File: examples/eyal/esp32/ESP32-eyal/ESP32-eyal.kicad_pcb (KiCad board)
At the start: 2 copper layers, 47 x 45.7 mm, 30 parts, among them J1 Battery, J2 OW, J3 V1, J4 Serial, J5 VDD_I_SENSE, J6 BATT_I_SENSE, J7 ALT_V2, J8 ALT_V3, J9 Solar, Q1 2N7002W, Q2 DMP1045U, Q3 DMP1045U, Q4 DMP1045U, U1 RT9080-33, U2 ESP32-WROOM-32, U3 MCP73831

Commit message: Commit recent updates
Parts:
- added R12: 10K, Resistor_SMD:R_0805_2012Metric, F.Cu at (98.4, 107.3)
- J4: footprint Connector_PinHeader_2.54mm:PinHeader_1x03_P2.54mm_Vertical -> Connector_PinHeader_2.54mm:PinHeader_1x05_P2.54mm_Vertical
- moved J4 5.12 mm to (139.1, 139.1)
- moved Program1 0.90 mm to (123.2, 125.1)
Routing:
- net /EN: track 24.0 -> 76.7 mm, vias 0 -> 1
- net /PGM: track 4.71 -> 24.5 mm, vias 0 -> 1
- net Net-(J4-Pad1): track 36.8 -> 41.4 mm
- net Net-(J4-Pad3): track 31.1 -> 35.6 mm
- net /SOLAR: track 7.41 -> 9.26 mm
- net VDD: track 107.0 -> 108.7 mm
- net /V1: track 42.6 -> 43.9 mm
- net +BATT: track 77.3 -> 78.5 mm
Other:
- board text added: "DTR"
- board text added: "RTS"

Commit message: some minor pcb adjustments (clear DRC warnings).
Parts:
- moved R10 0.64 mm to (139.7, 124.5)
- moved R7 0.64 mm to (137.2, 124.5)
- moved J4 0.63 mm to (139.1, 138.4)
- renumbered Program1 to pgm, Reset1 to rst
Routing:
- net Net-(J4-Pad1): track 41.4 -> 39.1 mm
- net Net-(J4-Pad3): track 35.6 -> 33.5 mm
- net GND: track 213.2 -> 211.6 mm
- net +BATT: track 78.5 -> 76.9 mm
- net /VDD_SENSE: track 51.3 -> 49.9 mm
- net VDD: track 108.7 -> 107.5 mm
- net /VBAT_SENSE: track 46.1 -> 47.2 mm
- net /V1_SENSE: track 53.9 -> 53.2 mm
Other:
- board size 47 x 45.7 mm -> 47.6 x 46.4 mm
- board text added: "SCL"
- board text added: "SDA"
- board text added: "SOLR"
- board text removed: "OW"

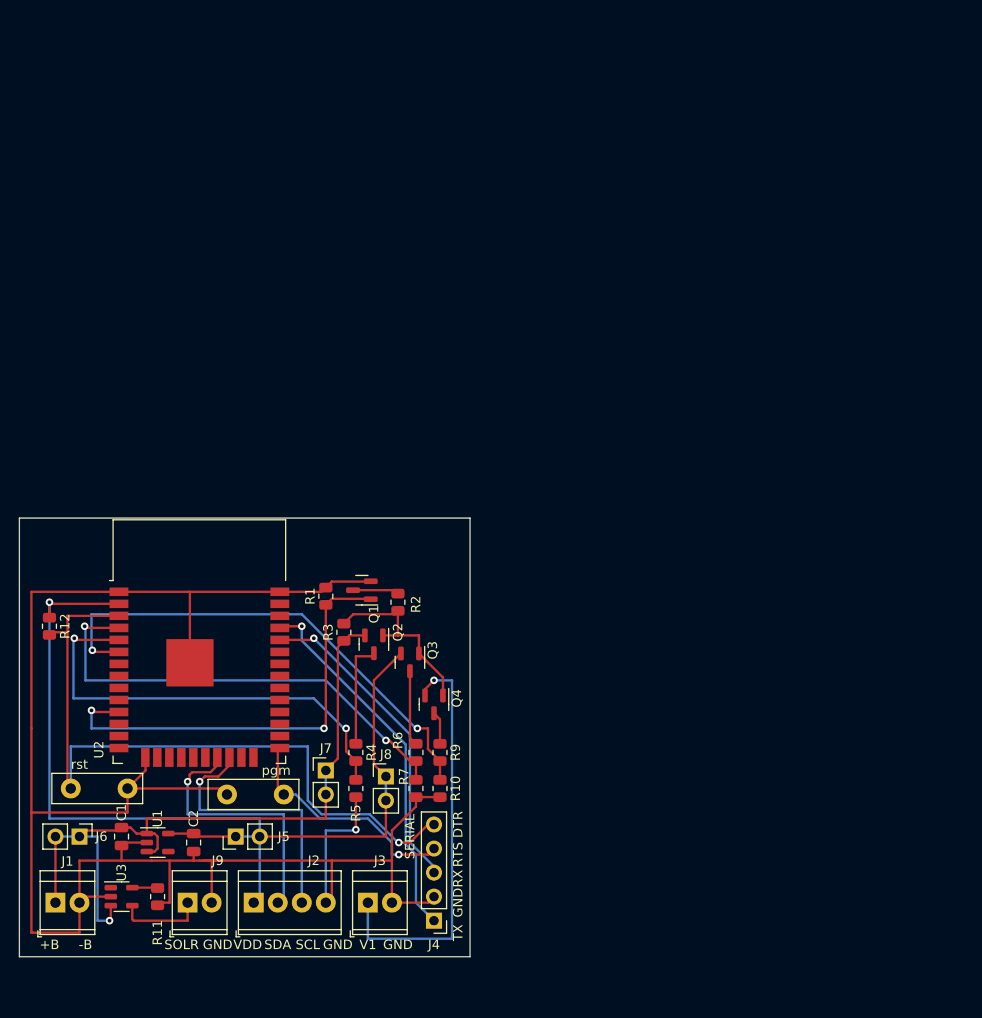
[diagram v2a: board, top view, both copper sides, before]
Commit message: Same ESP pcb with many other small sot-23 adapters.
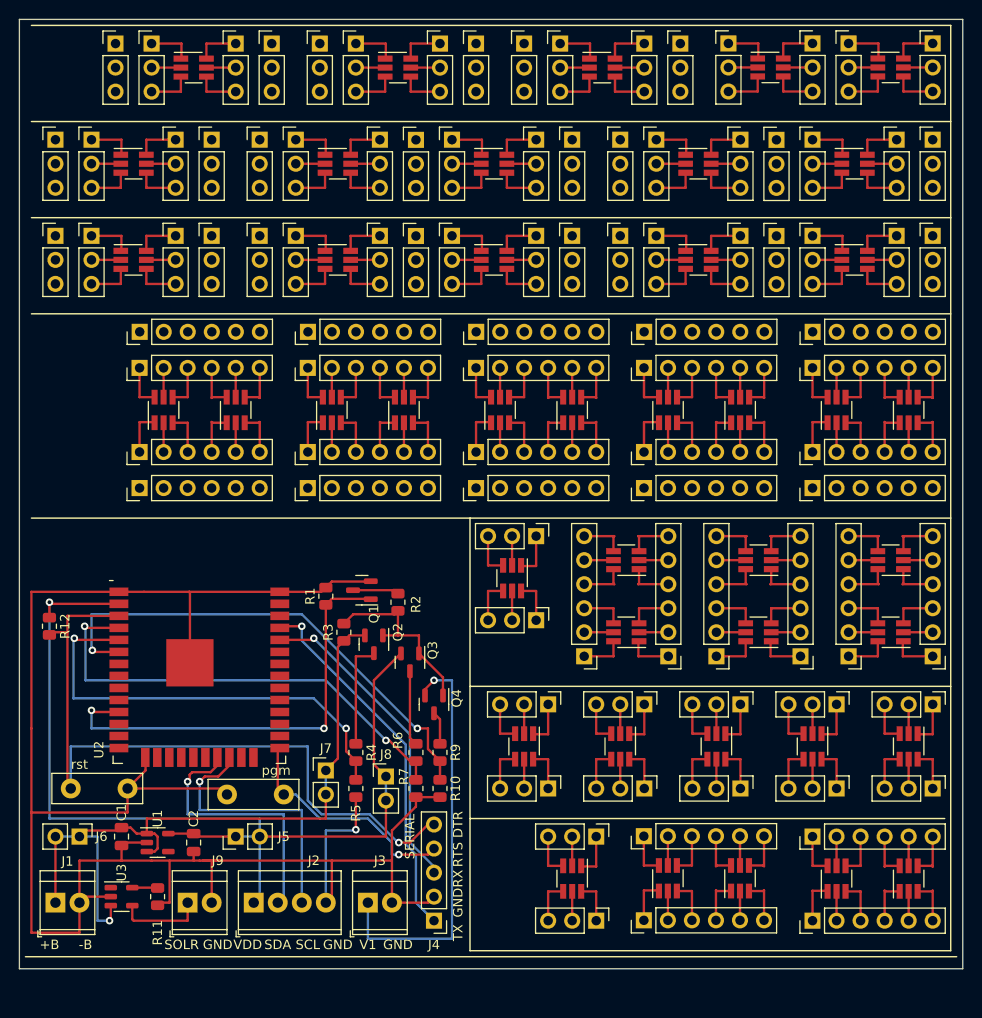
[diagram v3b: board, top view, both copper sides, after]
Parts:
- added REF**: PinHeader_1x03_P2.54mm_Vertical, Connector_PinHeader_2.54mm:PinHeader_1x03_P2.54mm_Vertical, F.Cu at (161.3, 115.6)
- added REF**: PinHeader_1x06_P2.54mm_Vertical, Connector_PinHeader_2.54mm:PinHeader_1x06_P2.54mm_Vertical, F.Cu at (108.0, 88.9)
- added REF**: PinHeader_1x03_P2.54mm_Vertical, Connector_PinHeader_2.54mm:PinHeader_1x03_P2.54mm_Vertical, F.Cu at (156.2, 138.4)
- added REF**: PinHeader_1x03_P2.54mm_Vertical, Connector_PinHeader_2.54mm:PinHeader_1x03_P2.54mm_Vertical, F.Cu at (162.6, 66.1)
- added REF**: PinHeader_1x03_P2.54mm_Vertical, Connector_PinHeader_2.54mm:PinHeader_1x03_P2.54mm_Vertical, F.Cu at (102.9, 55.9)
- added REF**: PinHeader_1x06_P2.54mm_Vertical, Connector_PinHeader_2.54mm:PinHeader_1x06_P2.54mm_Vertical, F.Cu at (161.2, 138.4)
- added REF**: PinHeader_1x06_P2.54mm_Vertical, Connector_PinHeader_2.54mm:PinHeader_1x06_P2.54mm_Vertical, F.Cu at (143.5, 80.0)
- added REF**: PinHeader_1x03_P2.54mm_Vertical, Connector_PinHeader_2.54mm:PinHeader_1x03_P2.54mm_Vertical, F.Cu at (149.9, 106.7)
- added REF**: PinHeader_1x06_P2.54mm_Vertical, Connector_PinHeader_2.54mm:PinHeader_1x06_P2.54mm_Vertical, F.Cu at (191.8, 110.5)
- added REF**: PinHeader_1x06_P2.54mm_Vertical, Connector_PinHeader_2.54mm:PinHeader_1x06_P2.54mm_Vertical, F.Cu at (182.9, 110.5)
- added REF**: PinHeader_1x03_P2.54mm_Vertical, Connector_PinHeader_2.54mm:PinHeader_1x03_P2.54mm_Vertical, F.Cu at (161.3, 124.5)
- added REF**: PinHeader_1x03_P2.54mm_Vertical, Connector_PinHeader_2.54mm:PinHeader_1x03_P2.54mm_Vertical, F.Cu at (124.5, 66.1)
- added REF**: SOT-23-6_Handsoldering, Package_TO_SOT_SMD:SOT-23-6_Handsoldering, F.Cu at (168.9, 120.0)
- added REF**: PinHeader_1x06_P2.54mm_Vertical, Connector_PinHeader_2.54mm:PinHeader_1x06_P2.54mm_Vertical, F.Cu at (179.1, 92.7)
- added REF**: PinHeader_1x03_P2.54mm_Vertical, Connector_PinHeader_2.54mm:PinHeader_1x03_P2.54mm_Vertical, F.Cu at (118.1, 45.7)
- added REF**: PinHeader_1x03_P2.54mm_Vertical, Connector_PinHeader_2.54mm:PinHeader_1x03_P2.54mm_Vertical, F.Cu at (171.4, 55.9)
- added REF**: SOT-23-6_Handsoldering, Package_TO_SOT_SMD:SOT-23-6_Handsoldering, F.Cu at (107.3, 58.4)
- added REF**: PinHeader_1x03_P2.54mm_Vertical, Connector_PinHeader_2.54mm:PinHeader_1x03_P2.54mm_Vertical, F.Cu at (191.8, 124.5)
- added REF**: PinHeader_1x06_P2.54mm_Vertical, Connector_PinHeader_2.54mm:PinHeader_1x06_P2.54mm_Vertical, F.Cu at (161.3, 92.7)
- added REF**: SOT-23-6_Handsoldering, Package_TO_SOT_SMD:SOT-23-6_Handsoldering, F.Cu at (128.9, 58.4)
- added REF**: SOT-23-6_Handsoldering, Package_TO_SOT_SMD:SOT-23-6_Handsoldering, F.Cu at (173.4, 108.0)
- added REF**: PinHeader_1x06_P2.54mm_Vertical, Connector_PinHeader_2.54mm:PinHeader_1x06_P2.54mm_Vertical, F.Cu at (179.1, 76.2)
- added REF**: SOT-23-6_Handsoldering, Package_TO_SOT_SMD:SOT-23-6_Handsoldering, F.Cu at (135.9, 84.5)
- added REF**: SOT-23-6_Handsoldering, Package_TO_SOT_SMD:SOT-23-6_Handsoldering, F.Cu at (163.8, 84.5)
- added REF**: PinHeader_1x03_P2.54mm_Vertical, Connector_PinHeader_2.54mm:PinHeader_1x03_P2.54mm_Vertical, F.Cu at (182.9, 45.7)
- added REF**: PinHeader_1x03_P2.54mm_Vertical, Connector_PinHeader_2.54mm:PinHeader_1x03_P2.54mm_Vertical, F.Cu at (161.3, 45.7)
- added REF**: PinHeader_1x03_P2.54mm_Vertical, Connector_PinHeader_2.54mm:PinHeader_1x03_P2.54mm_Vertical, F.Cu at (171.4, 66.1)
- added REF**: SOT-23-6_Handsoldering, Package_TO_SOT_SMD:SOT-23-6_Handsoldering, F.Cu at (118.1, 84.5)
- added REF**: PinHeader_1x06_P2.54mm_Vertical, Connector_PinHeader_2.54mm:PinHeader_1x06_P2.54mm_Vertical, F.Cu at (108.0, 76.2)
- added REF**: SOT-23-6_Handsoldering, Package_TO_SOT_SMD:SOT-23-6_Handsoldering, F.Cu at (147.3, 102.2)
- added REF**: PinHeader_1x03_P2.54mm_Vertical, Connector_PinHeader_2.54mm:PinHeader_1x03_P2.54mm_Vertical, F.Cu at (111.8, 55.9)
- added REF**: SOT-23-6_Handsoldering, Package_TO_SOT_SMD:SOT-23-6_Handsoldering, F.Cu at (179.1, 120.0)
- added REF**: PinHeader_1x03_P2.54mm_Vertical, Connector_PinHeader_2.54mm:PinHeader_1x03_P2.54mm_Vertical, F.Cu at (179.1, 55.9)
- added REF**: PinHeader_1x03_P2.54mm_Vertical, Connector_PinHeader_2.54mm:PinHeader_1x03_P2.54mm_Vertical, F.Cu at (139.7, 45.7)
- added REF**: PinHeader_1x06_P2.54mm_Vertical, Connector_PinHeader_2.54mm:PinHeader_1x06_P2.54mm_Vertical, F.Cu at (125.7, 88.9)
- added REF**: SOT-23-6_Handsoldering, Package_TO_SOT_SMD:SOT-23-6_Handsoldering, F.Cu at (173.4, 100.3)
- added REF**: PinHeader_1x03_P2.54mm_Vertical, Connector_PinHeader_2.54mm:PinHeader_1x03_P2.54mm_Vertical, F.Cu at (149.9, 55.9)
- added REF**: PinHeader_1x03_P2.54mm_Vertical, Connector_PinHeader_2.54mm:PinHeader_1x03_P2.54mm_Vertical, F.Cu at (99.1, 55.9)
- added REF**: PinHeader_1x03_P2.54mm_Vertical, Connector_PinHeader_2.54mm:PinHeader_1x03_P2.54mm_Vertical, F.Cu at (151.1, 124.5)
- added REF**: SOT-23-6_Handsoldering, Package_TO_SOT_SMD:SOT-23-6_Handsoldering, F.Cu at (187.3, 48.3)
- added REF**: SOT-23-6_Handsoldering, Package_TO_SOT_SMD:SOT-23-6_Handsoldering, F.Cu at (187.3, 100.3)
- added REF**: SOT-23-6_Handsoldering, Package_TO_SOT_SMD:SOT-23-6_Handsoldering, F.Cu at (110.5, 84.5)
- added REF**: PinHeader_1x06_P2.54mm_Vertical, Connector_PinHeader_2.54mm:PinHeader_1x06_P2.54mm_Vertical, F.Cu at (143.5, 92.7)
- added REF**: SOT-23-6_Handsoldering, Package_TO_SOT_SMD:SOT-23-6_Handsoldering, F.Cu at (128.9, 68.6)
- added REF**: SOT-23-6_Handsoldering, Package_TO_SOT_SMD:SOT-23-6_Handsoldering, F.Cu at (171.4, 84.5)
- added REF**: SOT-23-6_Handsoldering, Package_TO_SOT_SMD:SOT-23-6_Handsoldering, F.Cu at (153.7, 134.0)
- added REF**: PinHeader_1x03_P2.54mm_Vertical, Connector_PinHeader_2.54mm:PinHeader_1x03_P2.54mm_Vertical, F.Cu at (133.3, 66.1)
- added REF**: PinHeader_1x06_P2.54mm_Vertical, Connector_PinHeader_2.54mm:PinHeader_1x06_P2.54mm_Vertical, F.Cu at (154.9, 110.5)
- added REF**: SOT-23-6_Handsoldering, Package_TO_SOT_SMD:SOT-23-6_Handsoldering, F.Cu at (167.0, 58.4)
- added REF**: PinHeader_1x06_P2.54mm_Vertical, Connector_PinHeader_2.54mm:PinHeader_1x06_P2.54mm_Vertical, F.Cu at (179.1, 129.5)
- added REF**: PinHeader_1x06_P2.54mm_Vertical, Connector_PinHeader_2.54mm:PinHeader_1x06_P2.54mm_Vertical, F.Cu at (108.0, 92.7)
- added REF**: PinHeader_1x03_P2.54mm_Vertical, Connector_PinHeader_2.54mm:PinHeader_1x03_P2.54mm_Vertical, F.Cu at (141.0, 55.9)
- added REF**: PinHeader_1x03_P2.54mm_Vertical, Connector_PinHeader_2.54mm:PinHeader_1x03_P2.54mm_Vertical, F.Cu at (133.3, 55.9)
- added REF**: PinHeader_1x03_P2.54mm_Vertical, Connector_PinHeader_2.54mm:PinHeader_1x03_P2.54mm_Vertical, F.Cu at (179.1, 66.1)
- added REF**: PinHeader_1x03_P2.54mm_Vertical, Connector_PinHeader_2.54mm:PinHeader_1x03_P2.54mm_Vertical, F.Cu at (149.9, 97.8)
- added REF**: PinHeader_1x06_P2.54mm_Vertical, Connector_PinHeader_2.54mm:PinHeader_1x06_P2.54mm_Vertical, F.Cu at (161.3, 76.2)
- added REF**: PinHeader_1x06_P2.54mm_Vertical, Connector_PinHeader_2.54mm:PinHeader_1x06_P2.54mm_Vertical, F.Cu at (177.8, 110.5)
- added REF**: PinHeader_1x03_P2.54mm_Vertical, Connector_PinHeader_2.54mm:PinHeader_1x03_P2.54mm_Vertical, F.Cu at (181.6, 115.6)
- added REF**: PinHeader_1x06_P2.54mm_Vertical, Connector_PinHeader_2.54mm:PinHeader_1x06_P2.54mm_Vertical, F.Cu at (163.8, 110.5)
- added REF**: PinHeader_1x06_P2.54mm_Vertical, Connector_PinHeader_2.54mm:PinHeader_1x06_P2.54mm_Vertical, F.Cu at (143.5, 76.2)
- added REF**: SOT-23-6_Handsoldering, Package_TO_SOT_SMD:SOT-23-6_Handsoldering, F.Cu at (107.3, 68.6)
- added REF**: PinHeader_1x06_P2.54mm_Vertical, Connector_PinHeader_2.54mm:PinHeader_1x06_P2.54mm_Vertical, F.Cu at (161.3, 80.0)
- added REF**: PinHeader_1x03_P2.54mm_Vertical, Connector_PinHeader_2.54mm:PinHeader_1x03_P2.54mm_Vertical, F.Cu at (171.4, 124.5)
- added REF**: PinHeader_1x03_P2.54mm_Vertical, Connector_PinHeader_2.54mm:PinHeader_1x03_P2.54mm_Vertical, F.Cu at (181.6, 124.5)
- added REF**: PinHeader_1x03_P2.54mm_Vertical, Connector_PinHeader_2.54mm:PinHeader_1x03_P2.54mm_Vertical, F.Cu at (153.7, 55.9)
- added REF**: SOT-23-6_Handsoldering, Package_TO_SOT_SMD:SOT-23-6_Handsoldering, F.Cu at (145.4, 58.4)
- added REF**: SOT-23-6_Handsoldering, Package_TO_SOT_SMD:SOT-23-6_Handsoldering, F.Cu at (171.4, 133.9)
- added REF**: SOT-23-6_Handsoldering, Package_TO_SOT_SMD:SOT-23-6_Handsoldering, F.Cu at (189.2, 134.0)
- added REF**: SOT-23-6_Handsoldering, Package_TO_SOT_SMD:SOT-23-6_Handsoldering, F.Cu at (148.6, 120.0)
- added REF**: PinHeader_1x03_P2.54mm_Vertical, Connector_PinHeader_2.54mm:PinHeader_1x03_P2.54mm_Vertical, F.Cu at (153.7, 66.1)
- added REF**: SOT-23-6_Handsoldering, Package_TO_SOT_SMD:SOT-23-6_Handsoldering, F.Cu at (183.5, 58.4)
- added REF**: SOT-23-6_Handsoldering, Package_TO_SOT_SMD:SOT-23-6_Handsoldering, F.Cu at (159.4, 108.0)
- added REF**: PinHeader_1x06_P2.54mm_Vertical, Connector_PinHeader_2.54mm:PinHeader_1x06_P2.54mm_Vertical, F.Cu at (143.5, 88.9)
- added REF**: PinHeader_1x06_P2.54mm_Vertical, Connector_PinHeader_2.54mm:PinHeader_1x06_P2.54mm_Vertical, F.Cu at (161.3, 88.9)
- added REF**: SOT-23-6_Handsoldering, Package_TO_SOT_SMD:SOT-23-6_Handsoldering, F.Cu at (145.4, 68.6)
- added REF**: PinHeader_1x03_P2.54mm_Vertical, Connector_PinHeader_2.54mm:PinHeader_1x03_P2.54mm_Vertical, F.Cu at (170.2, 45.7)
- added REF**: PinHeader_1x03_P2.54mm_Vertical, Connector_PinHeader_2.54mm:PinHeader_1x03_P2.54mm_Vertical, F.Cu at (124.5, 55.9)
- added REF**: PinHeader_1x03_P2.54mm_Vertical, Connector_PinHeader_2.54mm:PinHeader_1x03_P2.54mm_Vertical, F.Cu at (109.2, 45.7)
- added REF**: PinHeader_1x06_P2.54mm_Vertical, Connector_PinHeader_2.54mm:PinHeader_1x06_P2.54mm_Vertical, F.Cu at (179.1, 80.0)
- added REF**: PinHeader_1x03_P2.54mm_Vertical, Connector_PinHeader_2.54mm:PinHeader_1x03_P2.54mm_Vertical, F.Cu at (121.9, 45.7)
- added REF**: PinHeader_1x03_P2.54mm_Vertical, Connector_PinHeader_2.54mm:PinHeader_1x03_P2.54mm_Vertical, F.Cu at (175.3, 55.9)
- added REF**: PinHeader_1x03_P2.54mm_Vertical, Connector_PinHeader_2.54mm:PinHeader_1x03_P2.54mm_Vertical, F.Cu at (171.4, 115.6)
- added REF**: PinHeader_1x06_P2.54mm_Vertical, Connector_PinHeader_2.54mm:PinHeader_1x06_P2.54mm_Vertical, F.Cu at (125.7, 76.2)
- added REF**: PinHeader_1x06_P2.54mm_Vertical, Connector_PinHeader_2.54mm:PinHeader_1x06_P2.54mm_Vertical, F.Cu at (125.7, 92.7)
- added REF**: PinHeader_1x03_P2.54mm_Vertical, Connector_PinHeader_2.54mm:PinHeader_1x03_P2.54mm_Vertical, F.Cu at (120.7, 66.1)
- added REF**: SOT-23-6_Handsoldering, Package_TO_SOT_SMD:SOT-23-6_Handsoldering, F.Cu at (156.8, 48.3)
- added REF**: PinHeader_1x03_P2.54mm_Vertical, Connector_PinHeader_2.54mm:PinHeader_1x03_P2.54mm_Vertical, F.Cu at (127.0, 45.7)
- added REF**: PinHeader_1x03_P2.54mm_Vertical, Connector_PinHeader_2.54mm:PinHeader_1x03_P2.54mm_Vertical, F.Cu at (162.6, 55.9)
- added REF**: PinHeader_1x03_P2.54mm_Vertical, Connector_PinHeader_2.54mm:PinHeader_1x03_P2.54mm_Vertical, F.Cu at (148.6, 45.7)
- added REF**: PinHeader_1x06_P2.54mm_Vertical, Connector_PinHeader_2.54mm:PinHeader_1x06_P2.54mm_Vertical, F.Cu at (179.1, 138.4)
- added REF**: PinHeader_1x03_P2.54mm_Vertical, Connector_PinHeader_2.54mm:PinHeader_1x03_P2.54mm_Vertical, F.Cu at (179.1, 45.7)
- added REF**: PinHeader_1x03_P2.54mm_Vertical, Connector_PinHeader_2.54mm:PinHeader_1x03_P2.54mm_Vertical, F.Cu at (115.6, 66.1)
- added REF**: PinHeader_1x03_P2.54mm_Vertical, Connector_PinHeader_2.54mm:PinHeader_1x03_P2.54mm_Vertical, F.Cu at (120.7, 55.9)
- added REF**: SOT-23-6_Handsoldering, Package_TO_SOT_SMD:SOT-23-6_Handsoldering, F.Cu at (183.5, 68.6)
- added REF**: PinHeader_1x03_P2.54mm_Vertical, Connector_PinHeader_2.54mm:PinHeader_1x03_P2.54mm_Vertical, F.Cu at (165.1, 45.7)
- added REF**: SOT-23-6_Handsoldering, Package_TO_SOT_SMD:SOT-23-6_Handsoldering, F.Cu at (187.3, 108.0)
- added REF**: PinHeader_1x03_P2.54mm_Vertical, Connector_PinHeader_2.54mm:PinHeader_1x03_P2.54mm_Vertical, F.Cu at (191.8, 55.9)
- added REF**: SOT-23-6_Handsoldering, Package_TO_SOT_SMD:SOT-23-6_Handsoldering, F.Cu at (158.8, 120.0)
- added REF**: SOT-23-6_Handsoldering, Package_TO_SOT_SMD:SOT-23-6_Handsoldering, F.Cu at (153.7, 84.5)
- added REF**: PinHeader_1x03_P2.54mm_Vertical, Connector_PinHeader_2.54mm:PinHeader_1x03_P2.54mm_Vertical, F.Cu at (102.9, 66.1)
- added REF**: PinHeader_1x03_P2.54mm_Vertical, Connector_PinHeader_2.54mm:PinHeader_1x03_P2.54mm_Vertical, F.Cu at (152.4, 45.7)
- added REF**: PinHeader_1x06_P2.54mm_Vertical, Connector_PinHeader_2.54mm:PinHeader_1x06_P2.54mm_Vertical, F.Cu at (168.9, 110.5)
- added REF**: PinHeader_1x03_P2.54mm_Vertical, Connector_PinHeader_2.54mm:PinHeader_1x03_P2.54mm_Vertical, F.Cu at (130.8, 45.7)
- added REF**: PinHeader_1x03_P2.54mm_Vertical, Connector_PinHeader_2.54mm:PinHeader_1x03_P2.54mm_Vertical, F.Cu at (149.9, 66.1)
- added REF**: PinHeader_1x03_P2.54mm_Vertical, Connector_PinHeader_2.54mm:PinHeader_1x03_P2.54mm_Vertical, F.Cu at (175.3, 66.1)
- added REF**: PinHeader_1x03_P2.54mm_Vertical, Connector_PinHeader_2.54mm:PinHeader_1x03_P2.54mm_Vertical, F.Cu at (115.6, 55.9)
- added REF**: PinHeader_1x03_P2.54mm_Vertical, Connector_PinHeader_2.54mm:PinHeader_1x03_P2.54mm_Vertical, F.Cu at (188.0, 55.9)
- added REF**: PinHeader_1x03_P2.54mm_Vertical, Connector_PinHeader_2.54mm:PinHeader_1x03_P2.54mm_Vertical, F.Cu at (141.0, 66.1)
- added REF**: PinHeader_1x06_P2.54mm_Vertical, Connector_PinHeader_2.54mm:PinHeader_1x06_P2.54mm_Vertical, F.Cu at (179.1, 88.9)
- added REF**: PinHeader_1x03_P2.54mm_Vertical, Connector_PinHeader_2.54mm:PinHeader_1x03_P2.54mm_Vertical, F.Cu at (105.4, 45.7)
- added REF**: SOT-23-6_Handsoldering, Package_TO_SOT_SMD:SOT-23-6_Handsoldering, F.Cu at (167.0, 68.6)
- added REF**: PinHeader_1x03_P2.54mm_Vertical, Connector_PinHeader_2.54mm:PinHeader_1x03_P2.54mm_Vertical, F.Cu at (137.2, 55.9)
- added REF**: PinHeader_1x03_P2.54mm_Vertical, Connector_PinHeader_2.54mm:PinHeader_1x03_P2.54mm_Vertical, F.Cu at (99.1, 66.1)
- added REF**: SOT-23-6_Handsoldering, Package_TO_SOT_SMD:SOT-23-6_Handsoldering, F.Cu at (189.2, 120.0)
- added REF**: PinHeader_1x03_P2.54mm_Vertical, Connector_PinHeader_2.54mm:PinHeader_1x03_P2.54mm_Vertical, F.Cu at (158.8, 66.1)
- added REF**: PinHeader_1x06_P2.54mm_Vertical, Connector_PinHeader_2.54mm:PinHeader_1x06_P2.54mm_Vertical, F.Cu at (125.7, 80.0)
- added REF**: SOT-23-6_Handsoldering, Package_TO_SOT_SMD:SOT-23-6_Handsoldering, F.Cu at (181.6, 134.0)
- added REF**: SOT-23-6_Handsoldering, Package_TO_SOT_SMD:SOT-23-6_Handsoldering, F.Cu at (128.3, 84.5)
- added REF**: PinHeader_1x03_P2.54mm_Vertical, Connector_PinHeader_2.54mm:PinHeader_1x03_P2.54mm_Vertical, F.Cu at (191.8, 66.1)
- added REF**: SOT-23-6_Handsoldering, Package_TO_SOT_SMD:SOT-23-6_Handsoldering, F.Cu at (174.6, 48.3)
- added REF**: PinHeader_1x06_P2.54mm_Vertical, Connector_PinHeader_2.54mm:PinHeader_1x06_P2.54mm_Vertical, F.Cu at (161.2, 129.5)
- added REF**: PinHeader_1x06_P2.54mm_Vertical, Connector_PinHeader_2.54mm:PinHeader_1x06_P2.54mm_Vertical, F.Cu at (108.0, 80.0)
- added REF**: SOT-23-6_Handsoldering, Package_TO_SOT_SMD:SOT-23-6_Handsoldering, F.Cu at (163.8, 133.9)
- added REF**: PinHeader_1x03_P2.54mm_Vertical, Connector_PinHeader_2.54mm:PinHeader_1x03_P2.54mm_Vertical, F.Cu at (156.2, 129.5)
- added REF**: PinHeader_1x03_P2.54mm_Vertical, Connector_PinHeader_2.54mm:PinHeader_1x03_P2.54mm_Vertical, F.Cu at (188.0, 66.1)
- added REF**: PinHeader_1x03_P2.54mm_Vertical, Connector_PinHeader_2.54mm:PinHeader_1x03_P2.54mm_Vertical, F.Cu at (158.8, 55.9)
- added REF**: PinHeader_1x03_P2.54mm_Vertical, Connector_PinHeader_2.54mm:PinHeader_1x03_P2.54mm_Vertical, F.Cu at (191.8, 115.6)
- added REF**: SOT-23-6_Handsoldering, Package_TO_SOT_SMD:SOT-23-6_Handsoldering, F.Cu at (159.4, 100.3)
- added REF**: PinHeader_1x03_P2.54mm_Vertical, Connector_PinHeader_2.54mm:PinHeader_1x03_P2.54mm_Vertical, F.Cu at (143.5, 45.7)
- added REF**: PinHeader_1x03_P2.54mm_Vertical, Connector_PinHeader_2.54mm:PinHeader_1x03_P2.54mm_Vertical, F.Cu at (111.8, 66.1)
- added REF**: SOT-23-6_Handsoldering, Package_TO_SOT_SMD:SOT-23-6_Handsoldering, F.Cu at (135.3, 48.3)
- added REF**: SOT-23-6_Handsoldering, Package_TO_SOT_SMD:SOT-23-6_Handsoldering, F.Cu at (113.7, 48.3)
- added REF**: PinHeader_1x03_P2.54mm_Vertical, Connector_PinHeader_2.54mm:PinHeader_1x03_P2.54mm_Vertical, F.Cu at (137.2, 66.1)
- added REF**: PinHeader_1x03_P2.54mm_Vertical, Connector_PinHeader_2.54mm:PinHeader_1x03_P2.54mm_Vertical, F.Cu at (191.8, 45.7)
- added REF**: PinHeader_1x03_P2.54mm_Vertical, Connector_PinHeader_2.54mm:PinHeader_1x03_P2.54mm_Vertical, F.Cu at (151.1, 115.6)
- added REF**: SOT-23-6_Handsoldering, Package_TO_SOT_SMD:SOT-23-6_Handsoldering, F.Cu at (146.1, 84.5)
- added REF**: SOT-23-6_Handsoldering, Package_TO_SOT_SMD:SOT-23-6_Handsoldering, F.Cu at (189.2, 84.5)
- added REF**: SOT-23-6_Handsoldering, Package_TO_SOT_SMD:SOT-23-6_Handsoldering, F.Cu at (181.6, 84.5)
- U2: footprint RF_Module:ESP32-WROOM-32 -> 0-Eyal:ESP32-WROOM-32
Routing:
- net (no net): track 0.00 -> 1054.5 mm
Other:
- board size 47.6 x 46.4 mm -> 99.7 x 100.3 mm

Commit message: Latest version, with mounting holes and a sea of small utility modules.
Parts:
- removed the REF** at (161.3, 115.6)
- removed the REF** at (108.0, 88.9)
- removed the REF** at (156.2, 138.4)
- removed the REF** at (162.6, 66.1)
- removed the REF** at (102.9, 55.9)
- removed the REF** at (161.2, 138.4)
- removed the REF** at (143.5, 80.0)
- removed the REF** at (149.9, 106.7)
- removed the REF** at (191.8, 110.5)
- removed the REF** at (182.9, 110.5)
- removed the REF** at (161.3, 124.5)
- removed the REF** at (124.5, 66.1)
- removed the REF** at (168.9, 120.0)
- removed the REF** at (179.1, 92.7)
- removed the REF** at (118.1, 45.7)
- removed the REF** at (171.4, 55.9)
- removed the REF** at (107.3, 58.4)
- removed the REF** at (191.8, 124.5)
- removed the REF** at (161.3, 92.7)
- removed the REF** at (128.9, 58.4)
- removed the REF** at (173.4, 108.0)
- removed the REF** at (179.1, 76.2)
- removed the REF** at (135.9, 84.5)
- removed the REF** at (163.8, 84.5)
- removed the REF** at (182.9, 45.7)
- removed the REF** at (161.3, 45.7)
- removed the REF** at (171.4, 66.1)
- removed the REF** at (118.1, 84.5)
- removed the REF** at (108.0, 76.2)
- removed the REF** at (147.3, 102.2)
- removed the REF** at (111.8, 55.9)
- removed the REF** at (179.1, 120.0)
- removed the REF** at (179.1, 55.9)
- removed the REF** at (139.7, 45.7)
- removed the REF** at (125.7, 88.9)
- removed the REF** at (173.4, 100.3)
- removed the REF** at (149.9, 55.9)
- removed the REF** at (99.1, 55.9)
- removed the REF** at (151.1, 124.5)
- removed the REF** at (187.3, 48.3)
- removed the REF** at (187.3, 100.3)
- removed the REF** at (110.5, 84.5)
- removed the REF** at (143.5, 92.7)
- removed the REF** at (128.9, 68.6)
- removed the REF** at (171.4, 84.5)
- removed the REF** at (153.7, 134.0)
- removed the REF** at (133.3, 66.1)
- removed the REF** at (154.9, 110.5)
- removed the REF** at (167.0, 58.4)
- removed the REF** at (179.1, 129.5)
- removed the REF** at (108.0, 92.7)
- removed the REF** at (141.0, 55.9)
- removed the REF** at (133.3, 55.9)
- removed the REF** at (179.1, 66.1)
- removed the REF** at (149.9, 97.8)
- removed the REF** at (161.3, 76.2)
- removed the REF** at (177.8, 110.5)
- removed the REF** at (181.6, 115.6)
- removed the REF** at (163.8, 110.5)
- removed the REF** at (143.5, 76.2)
- removed the REF** at (107.3, 68.6)
- removed the REF** at (161.3, 80.0)
- removed the REF** at (171.4, 124.5)
- removed the REF** at (181.6, 124.5)
- removed the REF** at (153.7, 55.9)
- removed the REF** at (145.4, 58.4)
- removed the REF** at (171.4, 133.9)
- removed the REF** at (189.2, 134.0)
- removed the REF** at (148.6, 120.0)
- removed the REF** at (153.7, 66.1)
- removed the REF** at (183.5, 58.4)
- removed the REF** at (159.4, 108.0)
- removed the REF** at (143.5, 88.9)
- removed the REF** at (161.3, 88.9)
- removed the REF** at (145.4, 68.6)
- removed the REF** at (170.2, 45.7)
- removed the REF** at (124.5, 55.9)
- removed the REF** at (109.2, 45.7)
- removed the REF** at (179.1, 80.0)
- removed the REF** at (121.9, 45.7)
- removed the REF** at (175.3, 55.9)
- removed the REF** at (171.4, 115.6)
- removed the REF** at (125.7, 76.2)
- removed the REF** at (125.7, 92.7)
- removed the REF** at (120.7, 66.1)
- removed the REF** at (156.8, 48.3)
- removed the REF** at (127.0, 45.7)
- removed the REF** at (162.6, 55.9)
- removed the REF** at (148.6, 45.7)
- removed the REF** at (179.1, 138.4)
- removed the REF** at (179.1, 45.7)
- removed the REF** at (115.6, 66.1)
- removed the REF** at (120.7, 55.9)
- removed the REF** at (183.5, 68.6)
- removed the REF** at (165.1, 45.7)
- removed the REF** at (187.3, 108.0)
- removed the REF** at (191.8, 55.9)
- removed the REF** at (158.8, 120.0)
- removed the REF** at (153.7, 84.5)
- removed the REF** at (102.9, 66.1)
- removed the REF** at (152.4, 45.7)
- removed the REF** at (168.9, 110.5)
- removed the REF** at (130.8, 45.7)
- removed the REF** at (149.9, 66.1)
- removed the REF** at (175.3, 66.1)
- removed the REF** at (115.6, 55.9)
- removed the REF** at (188.0, 55.9)
- removed the REF** at (141.0, 66.1)
- removed the REF** at (179.1, 88.9)
- removed the REF** at (105.4, 45.7)
- removed the REF** at (167.0, 68.6)
- removed the REF** at (137.2, 55.9)
- removed the REF** at (99.1, 66.1)
- removed the REF** at (189.2, 120.0)
- removed the REF** at (158.8, 66.1)
- removed the REF** at (125.7, 80.0)
- removed the REF** at (181.6, 134.0)
- removed the REF** at (128.3, 84.5)
- removed the REF** at (191.8, 66.1)
- removed the REF** at (174.6, 48.3)
- removed the REF** at (161.2, 129.5)
- removed the REF** at (108.0, 80.0)
- removed the REF** at (163.8, 133.9)
- removed the REF** at (156.2, 129.5)
- removed the REF** at (188.0, 66.1)
- removed the REF** at (158.8, 55.9)
- removed the REF** at (191.8, 115.6)
- removed the REF** at (159.4, 100.3)
- removed the REF** at (143.5, 45.7)
- removed the REF** at (111.8, 66.1)
- removed the REF** at (135.3, 48.3)
- removed the REF** at (113.7, 48.3)
- removed the REF** at (137.2, 66.1)
- removed the REF** at (191.8, 45.7)
- removed the REF** at (151.1, 115.6)
- removed the REF** at (146.1, 84.5)
- removed the REF** at (189.2, 84.5)
- removed the REF** at (181.6, 84.5)
- added REF**: PinHeader_1x03_P2.54mm_Vertical, Connector_PinHeader_2.54mm:PinHeader_1x03_P2.54mm_Vertical, F.Cu at (127.0, 50.2)
- added REF**: SOT-23-6_Handsoldering, Package_TO_SOT_SMD:SOT-23-6_Handsoldering, F.Cu at (145.4, 62.9)
- added REF**: PinHeader_1x06_P2.54mm_Vertical, Connector_PinHeader_2.54mm:PinHeader_1x06_P2.54mm_Vertical, F.Cu at (179.1, 97.2)
- added REF**: SOT-23-6_Handsoldering, Package_TO_SOT_SMD:SOT-23-6_Handsoldering, F.Cu at (167.0, 73.0)
- added REF**: PinHeader_1x03_P2.54mm_Vertical, Connector_PinHeader_2.54mm:PinHeader_1x03_P2.54mm_Vertical, F.Cu at (175.3, 60.4)
- added REF**: PinHeader_1x03_P2.54mm_Vertical, Connector_PinHeader_2.54mm:PinHeader_1x03_P2.54mm_Vertical, F.Cu at (179.1, 50.2)
- added REF**: PinHeader_1x03_P2.54mm_Vertical, Connector_PinHeader_2.54mm:PinHeader_1x03_P2.54mm_Vertical, F.Cu at (118.1, 50.2)
- added REF**: SOT-23-6_Handsoldering, Package_TO_SOT_SMD:SOT-23-6_Handsoldering, F.Cu at (181.6, 88.9)
- added REF**: PinHeader_1x06_P2.54mm_Vertical, Connector_PinHeader_2.54mm:PinHeader_1x06_P2.54mm_Vertical, F.Cu at (161.3, 80.6)
- added REF**: PinHeader_1x03_P2.54mm_Vertical, Connector_PinHeader_2.54mm:PinHeader_1x03_P2.54mm_Vertical, F.Cu at (150.2, 102.2)
- added REF**: PinHeader_1x03_P2.54mm_Vertical, Connector_PinHeader_2.54mm:PinHeader_1x03_P2.54mm_Vertical, F.Cu at (191.8, 120.0)
- added REF**: PinHeader_1x03_P2.54mm_Vertical, Connector_PinHeader_2.54mm:PinHeader_1x03_P2.54mm_Vertical, F.Cu at (105.4, 50.2)
- added REF**: PinHeader_1x03_P2.54mm_Vertical, Connector_PinHeader_2.54mm:PinHeader_1x03_P2.54mm_Vertical, F.Cu at (115.6, 60.3)
- added REF**: SOT-23-6_Handsoldering, Package_TO_SOT_SMD:SOT-23-6_Handsoldering, F.Cu at (153.7, 138.4)
- added REF**: SOT-23-6_Handsoldering, Package_TO_SOT_SMD:SOT-23-6_Handsoldering, F.Cu at (163.8, 138.4)
- added REF**: SOT-23-6_Handsoldering, Package_TO_SOT_SMD:SOT-23-6_Handsoldering, F.Cu at (128.9, 62.9)
- added REF**: SOT-23-6_Handsoldering, Package_TO_SOT_SMD:SOT-23-6_Handsoldering, F.Cu at (158.8, 124.5)
- added REF**: PinHeader_1x06_P2.54mm_Vertical, Connector_PinHeader_2.54mm:PinHeader_1x06_P2.54mm_Vertical, F.Cu at (191.8, 114.9)
- added REF**: SOT-23-6_Handsoldering, Package_TO_SOT_SMD:SOT-23-6_Handsoldering, F.Cu at (107.3, 62.9)
- added REF**: PinHeader_1x03_P2.54mm_Vertical, Connector_PinHeader_2.54mm:PinHeader_1x03_P2.54mm_Vertical, F.Cu at (149.9, 60.3)
- added REF**: SOT-23-6_Handsoldering, Package_TO_SOT_SMD:SOT-23-6_Handsoldering, F.Cu at (183.5, 62.9)
- added REF**: PinHeader_1x06_P2.54mm_Vertical, Connector_PinHeader_2.54mm:PinHeader_1x06_P2.54mm_Vertical, F.Cu at (108.0, 97.2)
- added REF**: SOT-23-6_Handsoldering, Package_TO_SOT_SMD:SOT-23-6_Handsoldering, F.Cu at (135.3, 52.7)
- added REF**: PinHeader_1x06_P2.54mm_Vertical, Connector_PinHeader_2.54mm:PinHeader_1x06_P2.54mm_Vertical, F.Cu at (143.5, 97.2)
- added REF**: PinHeader_1x03_P2.54mm_Vertical, Connector_PinHeader_2.54mm:PinHeader_1x03_P2.54mm_Vertical, F.Cu at (133.3, 60.3)
- added REF**: MountingHole_2.2mm_M2, MountingHole:MountingHole_2.2mm_M2, F.Cu at (140.3, 142.9)
- added REF**: MountingHole_2.2mm_M2, MountingHole:MountingHole_2.2mm_M2, F.Cu at (98.4, 142.9)
- added REF**: SOT-23-6_Handsoldering, Package_TO_SOT_SMD:SOT-23-6_Handsoldering, F.Cu at (153.7, 88.9)
- added REF**: PinHeader_1x03_P2.54mm_Vertical, Connector_PinHeader_2.54mm:PinHeader_1x03_P2.54mm_Vertical, F.Cu at (170.2, 50.2)
- added REF**: PinHeader_1x06_P2.54mm_Vertical, Connector_PinHeader_2.54mm:PinHeader_1x06_P2.54mm_Vertical, F.Cu at (161.2, 142.8)
- added REF**: SOT-23-6_Handsoldering, Package_TO_SOT_SMD:SOT-23-6_Handsoldering, F.Cu at (128.3, 88.9)
- added REF**: PinHeader_1x03_P2.54mm_Vertical, Connector_PinHeader_2.54mm:PinHeader_1x03_P2.54mm_Vertical, F.Cu at (152.4, 50.2)
- added REF**: SOT-23-6_Handsoldering, Package_TO_SOT_SMD:SOT-23-6_Handsoldering, F.Cu at (135.9, 88.9)
- added REF**: PinHeader_1x03_P2.54mm_Vertical, Connector_PinHeader_2.54mm:PinHeader_1x03_P2.54mm_Vertical, F.Cu at (137.2, 70.5)
- added REF**: PinHeader_1x03_P2.54mm_Vertical, Connector_PinHeader_2.54mm:PinHeader_1x03_P2.54mm_Vertical, F.Cu at (111.8, 70.5)
- added REF**: PinHeader_1x03_P2.54mm_Vertical, Connector_PinHeader_2.54mm:PinHeader_1x03_P2.54mm_Vertical, F.Cu at (133.3, 70.5)
- added REF**: PinHeader_1x03_P2.54mm_Vertical, Connector_PinHeader_2.54mm:PinHeader_1x03_P2.54mm_Vertical, F.Cu at (156.2, 142.9)
- added REF**: SOT-23-6_Handsoldering, Package_TO_SOT_SMD:SOT-23-6_Handsoldering, F.Cu at (146.1, 88.9)
- added REF**: PinHeader_1x03_P2.54mm_Vertical, Connector_PinHeader_2.54mm:PinHeader_1x03_P2.54mm_Vertical, F.Cu at (191.8, 128.9)
- added REF**: SOT-23-6_Handsoldering, Package_TO_SOT_SMD:SOT-23-6_Handsoldering, F.Cu at (183.5, 73.0)
- added REF**: PinHeader_1x03_P2.54mm_Vertical, Connector_PinHeader_2.54mm:PinHeader_1x03_P2.54mm_Vertical, F.Cu at (188.0, 70.5)
- added REF**: PinHeader_1x03_P2.54mm_Vertical, Connector_PinHeader_2.54mm:PinHeader_1x03_P2.54mm_Vertical, F.Cu at (182.9, 50.2)
- added REF**: PinHeader_1x03_P2.54mm_Vertical, Connector_PinHeader_2.54mm:PinHeader_1x03_P2.54mm_Vertical, F.Cu at (111.8, 60.3)
- added REF**: PinHeader_1x03_P2.54mm_Vertical, Connector_PinHeader_2.54mm:PinHeader_1x03_P2.54mm_Vertical, F.Cu at (175.3, 70.5)
- added REF**: PinHeader_1x06_P2.54mm_Vertical, Connector_PinHeader_2.54mm:PinHeader_1x06_P2.54mm_Vertical, F.Cu at (163.8, 114.9)
- added REF**: PinHeader_1x03_P2.54mm_Vertical, Connector_PinHeader_2.54mm:PinHeader_1x03_P2.54mm_Vertical, F.Cu at (181.6, 120.0)
- added REF**: SOT-23-6_Handsoldering, Package_TO_SOT_SMD:SOT-23-6_Handsoldering, F.Cu at (189.2, 124.5)
- added REF**: PinHeader_1x03_P2.54mm_Vertical, Connector_PinHeader_2.54mm:PinHeader_1x03_P2.54mm_Vertical, F.Cu at (158.8, 60.3)
- added REF**: PinHeader_1x03_P2.54mm_Vertical, Connector_PinHeader_2.54mm:PinHeader_1x03_P2.54mm_Vertical, F.Cu at (161.3, 128.9)
- added REF**: SOT-23-6_Handsoldering, Package_TO_SOT_SMD:SOT-23-6_Handsoldering, F.Cu at (187.3, 112.4)
- added REF**: PinHeader_1x03_P2.54mm_Vertical, Connector_PinHeader_2.54mm:PinHeader_1x03_P2.54mm_Vertical, F.Cu at (121.9, 50.2)
- added REF**: SOT-23-6_Handsoldering, Package_TO_SOT_SMD:SOT-23-6_Handsoldering, F.Cu at (174.6, 52.7)
- added REF**: PinHeader_1x03_P2.54mm_Vertical, Connector_PinHeader_2.54mm:PinHeader_1x03_P2.54mm_Vertical, F.Cu at (102.9, 60.3)
- added REF**: PinHeader_1x03_P2.54mm_Vertical, Connector_PinHeader_2.54mm:PinHeader_1x03_P2.54mm_Vertical, F.Cu at (120.7, 70.5)
- added REF**: PinHeader_1x03_P2.54mm_Vertical, Connector_PinHeader_2.54mm:PinHeader_1x03_P2.54mm_Vertical, F.Cu at (161.3, 50.2)
- added REF**: PinHeader_1x03_P2.54mm_Vertical, Connector_PinHeader_2.54mm:PinHeader_1x03_P2.54mm_Vertical, F.Cu at (124.5, 70.5)
- added REF**: PinHeader_1x03_P2.54mm_Vertical, Connector_PinHeader_2.54mm:PinHeader_1x03_P2.54mm_Vertical, F.Cu at (109.2, 50.2)
- added REF**: SOT-23-6_Handsoldering, Package_TO_SOT_SMD:SOT-23-6_Handsoldering, F.Cu at (107.3, 73.0)
- added REF**: PinHeader_1x06_P2.54mm_Vertical, Connector_PinHeader_2.54mm:PinHeader_1x06_P2.54mm_Vertical, F.Cu at (179.1, 142.9)
- added REF**: PinHeader_1x06_P2.54mm_Vertical, Connector_PinHeader_2.54mm:PinHeader_1x06_P2.54mm_Vertical, F.Cu at (125.7, 97.2)
- added REF**: SOT-23-6_Handsoldering, Package_TO_SOT_SMD:SOT-23-6_Handsoldering, F.Cu at (168.9, 124.5)
- added REF**: PinHeader_1x06_P2.54mm_Vertical, Connector_PinHeader_2.54mm:PinHeader_1x06_P2.54mm_Vertical, F.Cu at (125.7, 80.6)
- added REF**: SOT-23-6_Handsoldering, Package_TO_SOT_SMD:SOT-23-6_Handsoldering, F.Cu at (147.6, 106.6)
- added REF**: PinHeader_1x03_P2.54mm_Vertical, Connector_PinHeader_2.54mm:PinHeader_1x03_P2.54mm_Vertical, F.Cu at (115.6, 70.5)
- added REF**: PinHeader_1x03_P2.54mm_Vertical, Connector_PinHeader_2.54mm:PinHeader_1x03_P2.54mm_Vertical, F.Cu at (149.9, 70.5)
- added REF**: PinHeader_1x03_P2.54mm_Vertical, Connector_PinHeader_2.54mm:PinHeader_1x03_P2.54mm_Vertical, F.Cu at (156.2, 134.0)
- added REF**: PinHeader_1x03_P2.54mm_Vertical, Connector_PinHeader_2.54mm:PinHeader_1x03_P2.54mm_Vertical, F.Cu at (171.4, 120.0)
- added REF**: PinHeader_1x03_P2.54mm_Vertical, Connector_PinHeader_2.54mm:PinHeader_1x03_P2.54mm_Vertical, F.Cu at (120.7, 60.3)
- added REF**: PinHeader_1x03_P2.54mm_Vertical, Connector_PinHeader_2.54mm:PinHeader_1x03_P2.54mm_Vertical, F.Cu at (124.5, 60.3)
- added REF**: PinHeader_1x06_P2.54mm_Vertical, Connector_PinHeader_2.54mm:PinHeader_1x06_P2.54mm_Vertical, F.Cu at (161.3, 97.2)
- added REF**: SOT-23-6_Handsoldering, Package_TO_SOT_SMD:SOT-23-6_Handsoldering, F.Cu at (113.7, 52.7)
- added REF**: SOT-23-6_Handsoldering, Package_TO_SOT_SMD:SOT-23-6_Handsoldering, F.Cu at (187.3, 52.7)
- added REF**: PinHeader_1x03_P2.54mm_Vertical, Connector_PinHeader_2.54mm:PinHeader_1x03_P2.54mm_Vertical, F.Cu at (161.3, 120.0)
- added REF**: PinHeader_1x06_P2.54mm_Vertical, Connector_PinHeader_2.54mm:PinHeader_1x06_P2.54mm_Vertical, F.Cu at (177.8, 114.9)
- added REF**: PinHeader_1x03_P2.54mm_Vertical, Connector_PinHeader_2.54mm:PinHeader_1x03_P2.54mm_Vertical, F.Cu at (171.4, 128.9)
- added REF**: PinHeader_1x03_P2.54mm_Vertical, Connector_PinHeader_2.54mm:PinHeader_1x03_P2.54mm_Vertical, F.Cu at (150.2, 111.0)
- added REF**: PinHeader_1x06_P2.54mm_Vertical, Connector_PinHeader_2.54mm:PinHeader_1x06_P2.54mm_Vertical, F.Cu at (179.1, 84.5)
- added REF**: SOT-23-6_Handsoldering, Package_TO_SOT_SMD:SOT-23-6_Handsoldering, F.Cu at (159.4, 112.4)
- added REF**: PinHeader_1x03_P2.54mm_Vertical, Connector_PinHeader_2.54mm:PinHeader_1x03_P2.54mm_Vertical, F.Cu at (151.1, 128.9)
- added REF**: PinHeader_1x03_P2.54mm_Vertical, Connector_PinHeader_2.54mm:PinHeader_1x03_P2.54mm_Vertical, F.Cu at (162.6, 70.5)
- added REF**: PinHeader_1x06_P2.54mm_Vertical, Connector_PinHeader_2.54mm:PinHeader_1x06_P2.54mm_Vertical, F.Cu at (168.9, 114.9)
- added REF**: PinHeader_1x03_P2.54mm_Vertical, Connector_PinHeader_2.54mm:PinHeader_1x03_P2.54mm_Vertical, F.Cu at (171.4, 70.5)
- added REF**: MountingHole_2.2mm_M2, MountingHole:MountingHole_2.2mm_M2, F.Cu at (98.4, 102.2)
- added REF**: PinHeader_1x03_P2.54mm_Vertical, Connector_PinHeader_2.54mm:PinHeader_1x03_P2.54mm_Vertical, F.Cu at (153.7, 70.5)
- added REF**: PinHeader_1x06_P2.54mm_Vertical, Connector_PinHeader_2.54mm:PinHeader_1x06_P2.54mm_Vertical, F.Cu at (161.2, 133.9)
- added REF**: PinHeader_1x06_P2.54mm_Vertical, Connector_PinHeader_2.54mm:PinHeader_1x06_P2.54mm_Vertical, F.Cu at (161.3, 93.3)
- added REF**: SOT-23-6_Handsoldering, Package_TO_SOT_SMD:SOT-23-6_Handsoldering, F.Cu at (173.4, 104.8)
- added REF**: PinHeader_1x03_P2.54mm_Vertical, Connector_PinHeader_2.54mm:PinHeader_1x03_P2.54mm_Vertical, F.Cu at (148.6, 50.2)
- added REF**: SOT-23-6_Handsoldering, Package_TO_SOT_SMD:SOT-23-6_Handsoldering, F.Cu at (163.8, 88.9)
- added REF**: PinHeader_1x06_P2.54mm_Vertical, Connector_PinHeader_2.54mm:PinHeader_1x06_P2.54mm_Vertical, F.Cu at (143.5, 84.5)
- added REF**: SOT-23-6_Handsoldering, Package_TO_SOT_SMD:SOT-23-6_Handsoldering, F.Cu at (173.4, 112.4)
- added REF**: PinHeader_1x03_P2.54mm_Vertical, Connector_PinHeader_2.54mm:PinHeader_1x03_P2.54mm_Vertical, F.Cu at (179.1, 70.5)
- added REF**: PinHeader_1x06_P2.54mm_Vertical, Connector_PinHeader_2.54mm:PinHeader_1x06_P2.54mm_Vertical, F.Cu at (108.0, 84.5)
- added REF**: PinHeader_1x03_P2.54mm_Vertical, Connector_PinHeader_2.54mm:PinHeader_1x03_P2.54mm_Vertical, F.Cu at (99.1, 60.3)
- added REF**: PinHeader_1x03_P2.54mm_Vertical, Connector_PinHeader_2.54mm:PinHeader_1x03_P2.54mm_Vertical, F.Cu at (191.8, 50.2)
- added REF**: PinHeader_1x03_P2.54mm_Vertical, Connector_PinHeader_2.54mm:PinHeader_1x03_P2.54mm_Vertical, F.Cu at (181.6, 128.9)
- added REF**: SOT-23-6_Handsoldering, Package_TO_SOT_SMD:SOT-23-6_Handsoldering, F.Cu at (167.0, 62.9)
- added REF**: PinHeader_1x06_P2.54mm_Vertical, Connector_PinHeader_2.54mm:PinHeader_1x06_P2.54mm_Vertical, F.Cu at (143.5, 80.6)
- added REF**: PinHeader_1x03_P2.54mm_Vertical, Connector_PinHeader_2.54mm:PinHeader_1x03_P2.54mm_Vertical, F.Cu at (130.8, 50.2)
- added REF**: PinHeader_1x06_P2.54mm_Vertical, Connector_PinHeader_2.54mm:PinHeader_1x06_P2.54mm_Vertical, F.Cu at (143.5, 93.3)
- added REF**: PinHeader_1x03_P2.54mm_Vertical, Connector_PinHeader_2.54mm:PinHeader_1x03_P2.54mm_Vertical, F.Cu at (141.0, 70.5)
- added REF**: PinHeader_1x06_P2.54mm_Vertical, Connector_PinHeader_2.54mm:PinHeader_1x06_P2.54mm_Vertical, F.Cu at (161.3, 84.5)
- added REF**: PinHeader_1x03_P2.54mm_Vertical, Connector_PinHeader_2.54mm:PinHeader_1x03_P2.54mm_Vertical, F.Cu at (139.7, 50.2)
- added REF**: PinHeader_1x06_P2.54mm_Vertical, Connector_PinHeader_2.54mm:PinHeader_1x06_P2.54mm_Vertical, F.Cu at (179.1, 93.3)
- added REF**: PinHeader_1x03_P2.54mm_Vertical, Connector_PinHeader_2.54mm:PinHeader_1x03_P2.54mm_Vertical, F.Cu at (188.0, 60.3)
- added REF**: PinHeader_1x03_P2.54mm_Vertical, Connector_PinHeader_2.54mm:PinHeader_1x03_P2.54mm_Vertical, F.Cu at (143.5, 50.2)
- added REF**: SOT-23-6_Handsoldering, Package_TO_SOT_SMD:SOT-23-6_Handsoldering, F.Cu at (110.5, 88.9)
- added REF**: PinHeader_1x06_P2.54mm_Vertical, Connector_PinHeader_2.54mm:PinHeader_1x06_P2.54mm_Vertical, F.Cu at (179.1, 134.0)
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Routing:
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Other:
- board size 99.7 x 100.3 mm -> 99.7 x 99.7 mm
